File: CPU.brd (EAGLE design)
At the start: 106.7 x 34 mm, 6 parts, among them IC1 Z80CPU

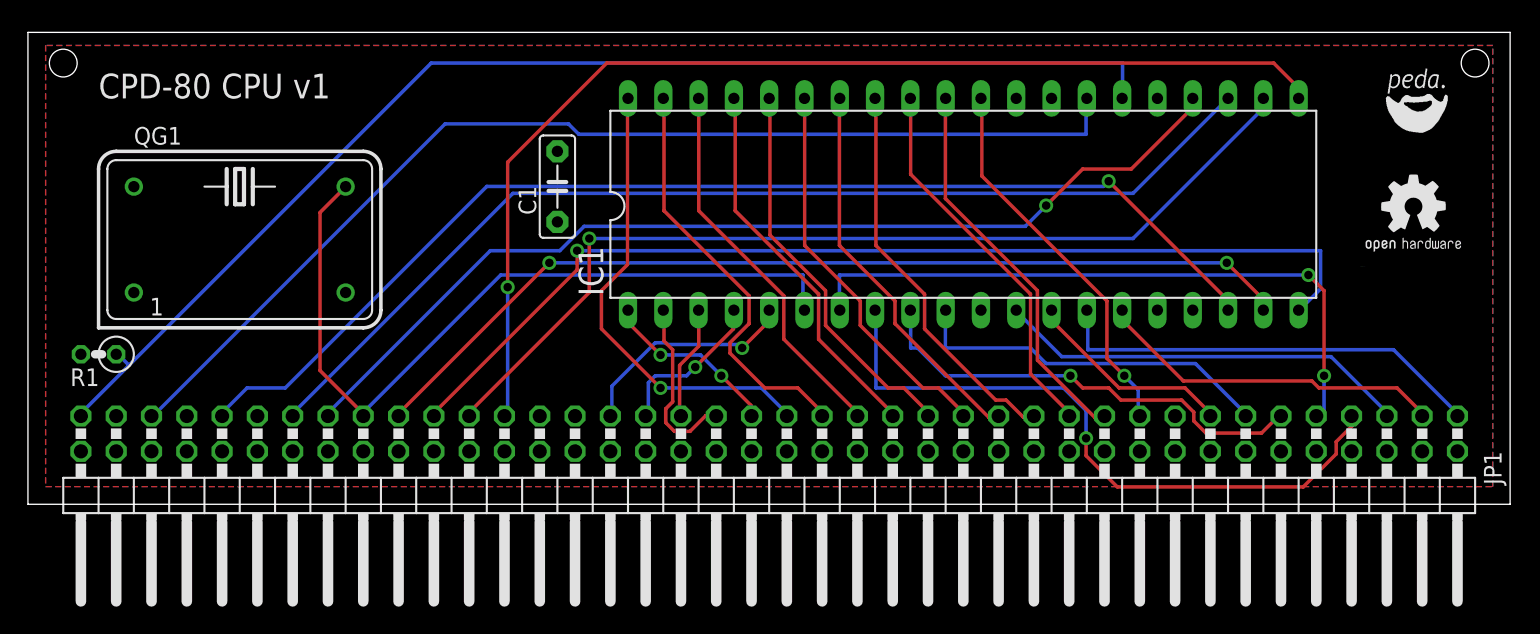
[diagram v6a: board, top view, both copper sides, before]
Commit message: Add PullUps to CPU Board
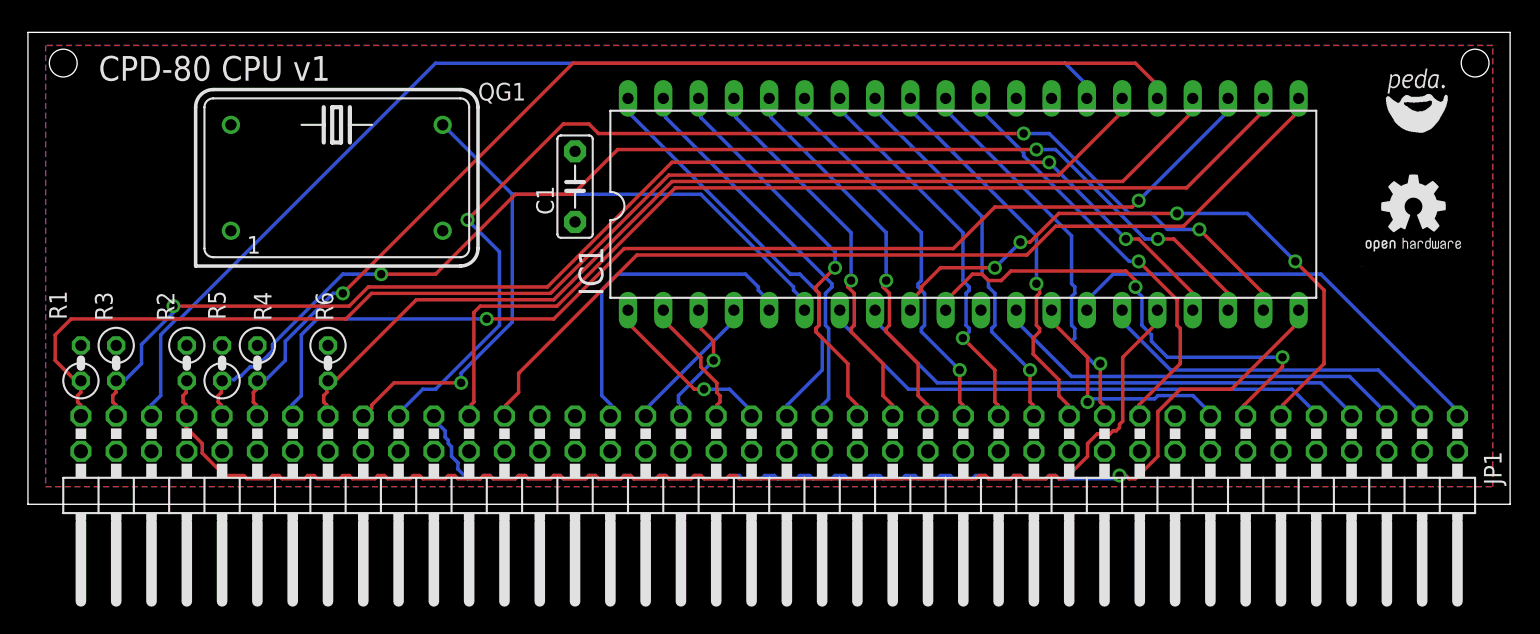
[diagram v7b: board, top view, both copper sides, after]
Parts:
- added R2, R3, R4, R5, R6: 3.3k, resistor:0207/2V
- moved QG1 8.28 mm to (21.0, 23.5)
- moved R1 1.42 mm to (2.54, 10.2), turned to 90 degrees
- moved C1 1.27 mm to (38.1, 22.9)
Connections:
- new net N$2: IC1.25, JP1.69, R4.2
- new net N$3: IC1.17, JP1.77, R3.2
- new net N$4: IC1.16, JP1.73, R2.2
- net N$9: now also R5.1
- net VCC: now also R2.1, R3.1, R4.1, R5.2, R6.1; no longer IC1.16, IC1.17, IC1.25, JP1.69, JP1.73, JP1.77
- net WAIT: now also R6.2
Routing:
- net N$3: track 0.00 -> 92.9 mm, vias 0 -> 3
- net N$4: track 0.00 -> 87.6 mm
- net N$2: track 0.00 -> 79.5 mm, vias 0 -> 1
- net N$8: track 68.8 -> 85.1 mm, vias 2 -> 3
- net D5: track 32.8 -> 45.8 mm, vias 1 -> 4
- net N$14: track 79.8 -> 68.4 mm, vias 1 -> 0
- net D3: track 47.8 -> 38.1 mm, vias 1 -> 0
- net D6: track 26.5 -> 36.1 mm, vias 0 -> 2
- net D4: track 47.4 -> 38.1 mm, vias 2 -> 0
- net A15: track 16.6 -> 23.5 mm, vias 1 -> 0
- net N$9: track 83.8 -> 87.8 mm, vias 1 -> 3
- net N$1: track 78.9 -> 82.6 mm
- net N$22: track 76.9 -> 80.6 mm, vias 0 -> 2
- net A12: track 13.0 -> 9.41 mm
- net A10: track 33.4 -> 30.4 mm, vias 1 -> 0
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
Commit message: Restructure CPU Schematic
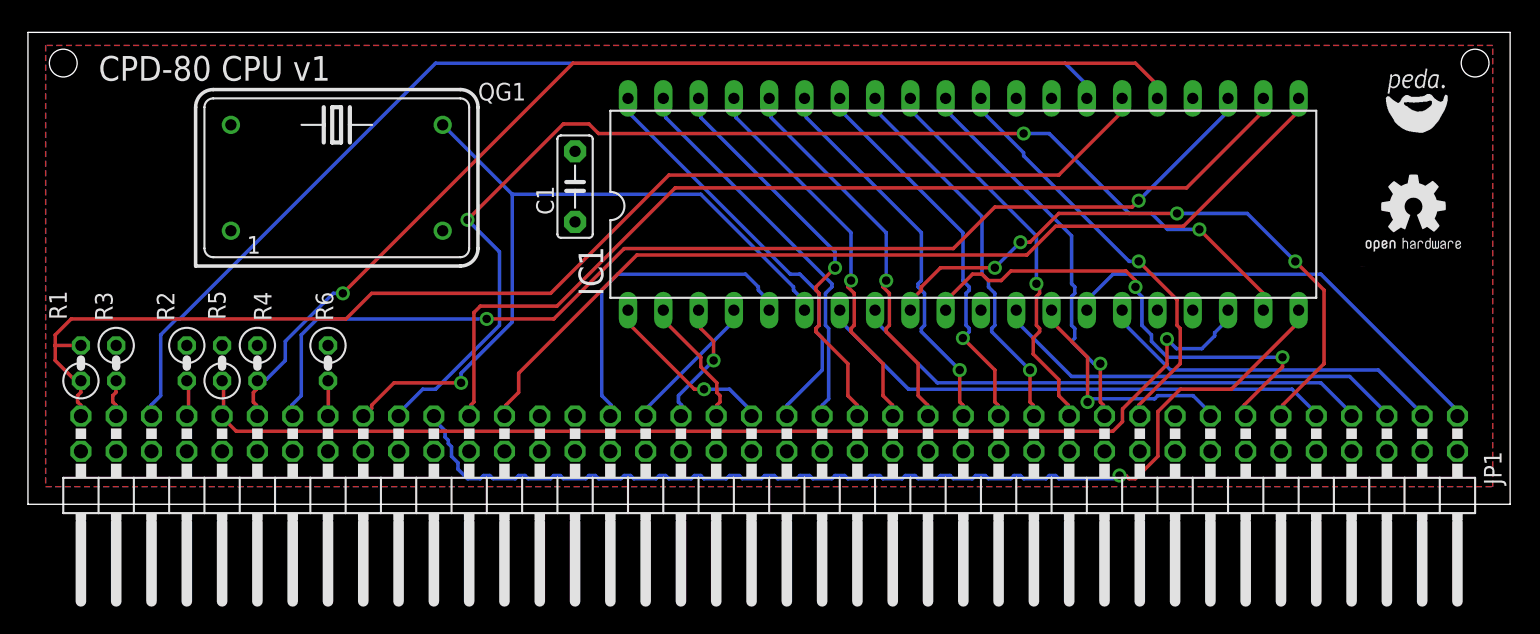
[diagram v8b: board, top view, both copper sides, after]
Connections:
- net CLOCK renamed CLK
- net N$1 renamed !M1
- net N$10 renamed !WR
- net N$14 renamed !RD
- net N$16 renamed !IORQ
- net N$2 renamed !BUSRQ
- net N$22 renamed !BUSAK
- net N$8 renamed !MREQ
- net N$9 renamed !HALT
- removed net N$3: IC1.17, JP1.77, R3.2
- removed net N$4: IC1.16, JP1.73, R2.2
- removed net WAIT: IC1.24, JP1.65, R6.2
- new net !INT: JP1.73, R2.2
- new net !NMI: JP1.77, R3.2
- new net !WAIT: JP1.65, R6.2
- net !RESET: now also R1.2; no longer IC1.26, R1.1
- net VCC: now also R1.1; no longer R1.2
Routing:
- net N$3: track 92.9 -> 0.00 mm, vias 3 -> 0
- net N$4: track 87.6 -> 0.00 mm
- net WAIT: track 74.1 -> 0.00 mm
- net !HALT: track 87.8 -> 81.8 mm, vias 3 -> 1
- net !NMI: track 0.00 -> 2.82 mm
- net !INT: track 0.00 -> 2.66 mm
- net !WAIT: track 0.00 -> 2.55 mm
- net !RESET: track 92.1 -> 93.2 mm
